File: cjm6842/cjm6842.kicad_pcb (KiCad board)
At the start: 2 copper layers, 114.3 x 88.9 mm, 52 parts, among them J1 AudioJack, J2 Speaker, J3 UART1, J4 Pot, J5 Conn_01x08_Pin, J6 GND, J7 DACOUT, J8 Joystick, J9 Joystick, SW1 UP, SW2 LEFT, SW3 DOWN, SW4 RGHT, U2 LP-MSPM0G3507, U3 MCP34119P, U4 HiLetGo_ST7735R, U5 ULN2003B, U6 TSOP31438

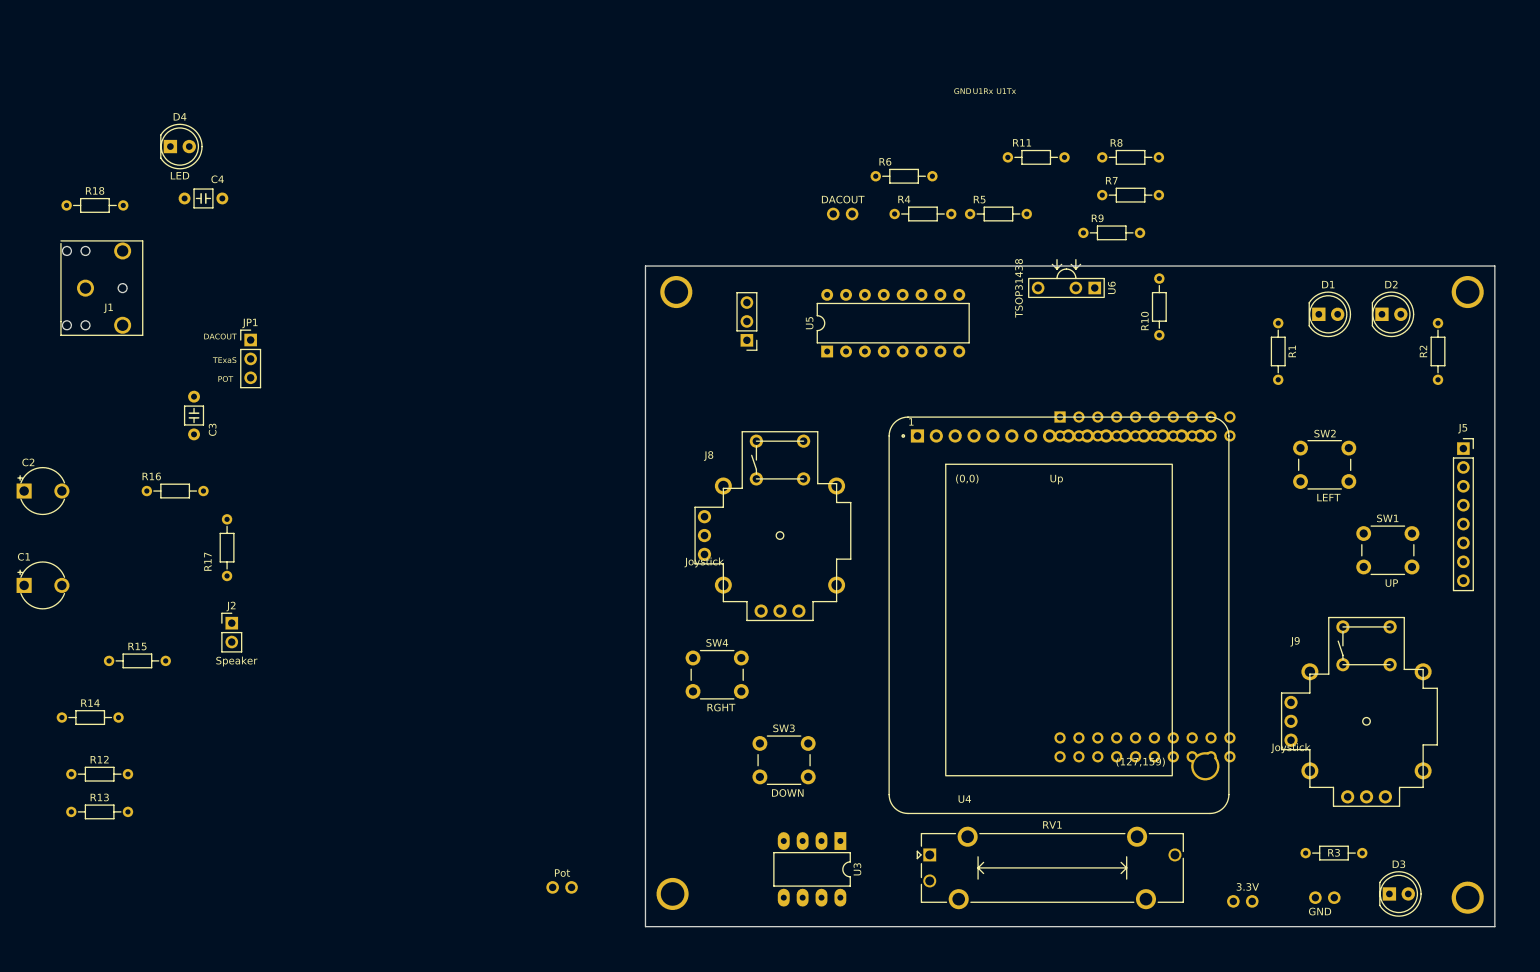
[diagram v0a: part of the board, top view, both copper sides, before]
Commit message: Rotated LCD; rearranged DAC
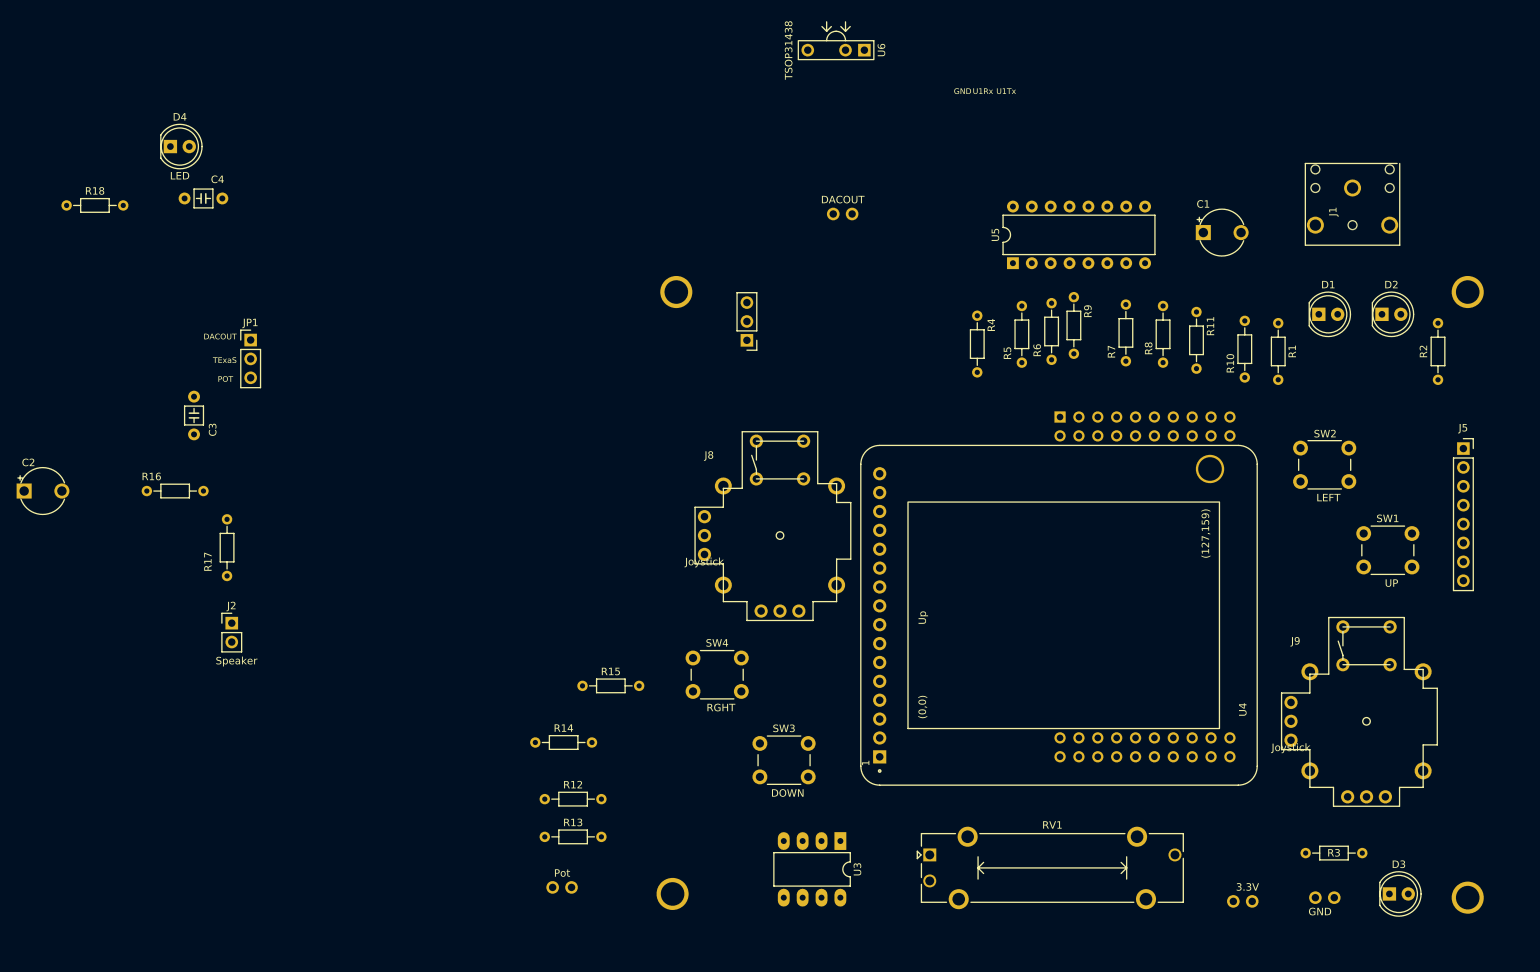
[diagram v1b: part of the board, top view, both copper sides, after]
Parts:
- moved J1 171.0 mm to (194.0, 40.5), turned to 180 degrees
- moved C1 165.6 mm to (173.9, 46.5)
- moved R14 63.8 mm to (91.7, 115.1)
- moved R12 63.8 mm to (92.9, 122.7)
- moved R13 63.8 mm to (92.9, 127.8)
- moved R15 63.8 mm to (98.0, 107.5)
- moved U6 44.6 mm to (128.3, 22.0)
- moved R6 34.2 mm to (153.5, 63.6), turned to 90 degrees
- moved R11 32.8 mm to (173.0, 57.2), turned to -90 degrees
- moved R8 28.8 mm to (168.5, 64.0), turned to 90 degrees
- moved U5 27.7 mm to (148.3, 50.6)
- moved R7 22.6 mm to (163.5, 63.8), turned to 90 degrees
- moved R5 21.2 mm to (149.5, 64.0), turned to 90 degrees
- moved R4 17.6 mm to (143.5, 57.7), turned to -90 degrees
- moved R10 12.8 mm to (179.5, 66.0)
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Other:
- board outline removed

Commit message: Layed wires for PCB
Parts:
- removed J1: AudioJack, ECE319K:Jack_3.5mm_CUI_SJ1-3523N_Horizontal
- moved R18 163.7 mm to (154.9, 137.0)
- moved C2 157.9 mm to (165.9, 128.5)
- moved D4 148.0 mm to (128.0, 150.0)
- moved G*** 144.6 mm to (111.0, 149.0)
- moved J2 142.8 mm to (178.5, 53.5), turned to 180 degrees
- moved R17 134.0 mm to (173.5, 64.3)
- moved R16 132.7 mm to (161.7, 54.5)
- moved C3 127.7 mm to (165.4, 59.4)
- moved C4 95.6 mm to (131.6, 54.6), turned to 90 degrees
- moved JP1 94.7 mm to (138.3, 41.0)
- moved R1 89.6 mm to (133.2, 132.5), turned to 0 degrees
- moved D1 87.6 mm to (135.5, 126.5)
- moved D2 86.8 mm to (145.2, 126.5)
- moved R2 84.9 mm to (152.3, 132.5), turned to 180 degrees
- moved J4 84.0 mm to (170.0, 143.0)
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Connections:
- J8 pad 5: PB17 -> PA24
- R15 pad 1: PA24 -> PB17
- SW4 pad 1: PA24 -> PB17
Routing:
- net +3V3: track 0.00 -> 407.6 mm, vias 0 -> 6
- net GND: track 0.00 -> 331.6 mm, vias 0 -> 2
- net PB18: track 0.00 -> 259.8 mm, vias 0 -> 3
- net PA17: track 0.00 -> 178.1 mm
- net PA31: track 0.00 -> 162.4 mm
- net +5V: track 0.00 -> 141.3 mm, vias 0 -> 3
- net Net-(U3-VO1): track 0.00 -> 137.4 mm
- net PA27: track 0.00 -> 123.7 mm, vias 0 -> 2
- net PA26: track 0.00 -> 119.3 mm
- net PA24: track 0.00 -> 114.7 mm, vias 0 -> 3
- net PA12: track 0.00 -> 111.3 mm, vias 0 -> 6
- net Net-(D4-K): track 0.00 -> 106.3 mm, vias 0 -> 2
- net PB24: track 0.00 -> 101.8 mm, vias 0 -> 7
- net Net-(U3-FC1): track 0.00 -> 95.2 mm, vias 0 -> 1
- net PB1: track 0.00 -> 94.3 mm, vias 0 -> 2
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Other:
- board outline added: 121 x 127.5 mm
- board text removed: "ECE319K PCB camp Spring 2025"
- board text removed: "GND"
- board text removed: "U1Rx"
- board text removed: "U1Tx"

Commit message: Completed PCB (I ordered this version)
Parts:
- removed J5: Conn_01x08_Pin, Connector_PinSocket_2.54mm:PinSocket_1x08_P2.54mm_Vertical
- removed J9: Joystick, ECE319K:SparkfunJoystick
- added R19: 10k, ECE319K:R_Axial_DIN0204_L3.6mm_D1.6mm_P7.62mm_Horizontal, F.Cu at (115.0, 152.0)
- added R20: 10k, ECE319K:R_Axial_DIN0204_L3.6mm_D1.6mm_P7.62mm_Horizontal, F.Cu at (191.8, 39.0)
- added RV2: PTA2043, ECE319K:PTA2043pot, F.Cu at (109.8, 97.9)
- added SW5: RGHT, ECE319K:SW_PUSH_6mm, F.Cu at (112.8, 144.2)
- added SW6: RGHT, ECE319K:SW_PUSH_6mm, F.Cu at (198.0, 45.5)
- J8: value Joystick -> Pot; footprint ECE319K:SparkfunJoystick -> ECE319K:Testpoint_1x02_P2.54mm
- moved G*** 98.1 mm to (110.3, 50.9)
- moved RV1 56.2 mm to (192.3, 129.6), turned to 90 degrees
- moved J8 29.0 mm to (113.5, 103.7), turned to -90 degrees
- moved SW4 3.55 mm to (108.8, 115.8)
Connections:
- J8 pad 1: GND -> PB19
- J8 pad 2: PB24 -> PB19
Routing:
- net PA24: track 114.7 -> 209.0 mm, vias 3 -> 4
- net PA28: track 78.7 -> 0.00 mm, vias 1 -> 0
- net PA25: track 75.4 -> 0.00 mm, vias 2 -> 0
- net GND: track 331.6 -> 382.9 mm, vias 2 -> 4
- net PA12: track 111.3 -> 71.6 mm, vias 6 -> 3
- net PB24: track 101.8 -> 129.2 mm, vias 7 -> 4
- net PB16: track 25.9 -> 0.00 mm
- net +3V3: track 407.6 -> 427.7 mm, vias 6 -> 8
- net PB17: track 84.3 -> 92.9 mm
- net PB18: track 259.8 -> 256.7 mm, vias 3 -> 5
- net PA17: track 178.1 -> 176.1 mm
- net PB19: track 79.6 -> 81.4 mm, vias 2 -> 3
- net PA15: track 74.8 -> 76.0 mm
- net PB8: track 60.7 -> 60.2 mm
- net PB6: track 63.3 -> 62.8 mm
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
